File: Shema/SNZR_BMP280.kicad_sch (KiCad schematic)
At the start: 8 parts, among them J1 Conn_01x06_Pin, U1 BMP280

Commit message: izmjena koda i dodavanje simbola konektora u projekt
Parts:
- removed J1: Conn_01x06_Pin, symbol Connector:Conn_01x06_Pin
- added J1: ~, symbol Symbol_Library:Konektor
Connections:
- net +3.3V: now also J1.1 (3.3V)
- net CSB: now also J1.5 (CSB)
- net GND: now also J1.2 (GND)
- net SCL: now also J1.3 (SCL)
- net SDA: now also J1.4 (SDA)
- net SDO: now also J1.6 (SD0)
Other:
- note added: "3V3 GND SCL - PB8 SDA - PB9 Not Connected Not Connected"
- note added: "Nucleo"

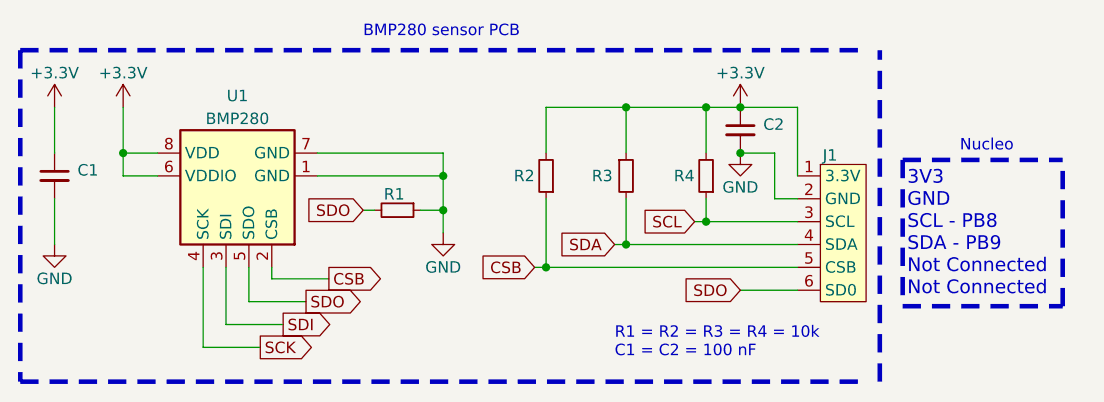
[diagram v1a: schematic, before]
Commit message: izmjenjen 3.3V na VCC na pinu konektora
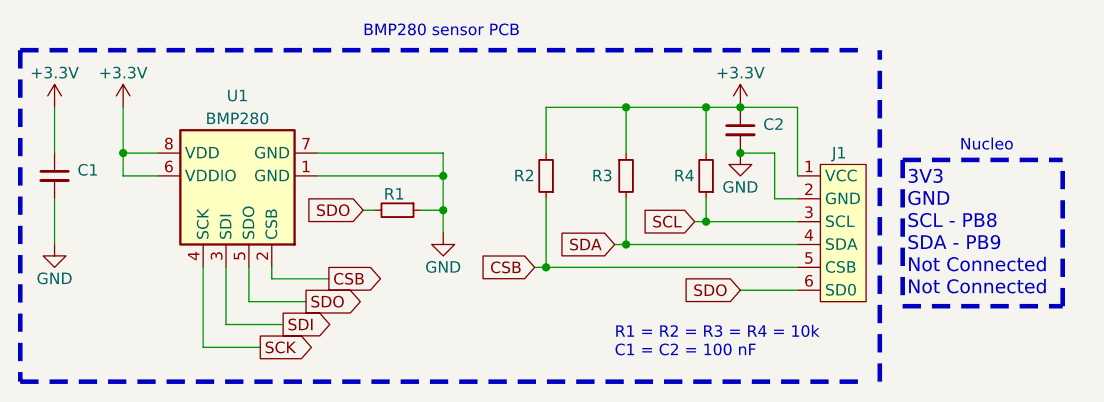
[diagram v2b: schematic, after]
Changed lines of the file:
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@@
+    )
+  )
+  (symbol (lib_name "Konektor_1") (lib_id "Symbol_Library:Konektor") (at 127 71.12 0) (unit 1)
+    (in_bom yes) (on_board yes) (dnp no)
+    (property "Reference" "J1" (at 125.73 62.23 0)
+      (effects (font (size 1.27 1.27)) (justify left))
+    )
+    (property "Value" "~" (at 121.92 60.96 0)
+      (effects (font (size 1.27 1.27)))
+    )
+    (property "Footprint" "" (at 121.92 60.96 0)
+      (effects (font (size 1.27 1.27)) hide)
+    )
+    (property "Datasheet" "" (at 121.92 60.96 0)
+      (effects (font (size 1.27 1.27)) hide)
+    )
+    (pin "1")
+    (pin "2")
+    (pin "3")
+    (pin "4")
+    (pin "5")
+    (pin "6")
+    (instances
+      (project "SNZR_BMP280"
+        (path "/09d5346e-2011-4469-84ee-b3a199e5e175"
+          (reference "J1") (unit 1)
+        )
+      )
     )
   )
@@
         )
       )
-    )
-  )
-  (symbol (lib_id "Symbol_Library:Konektor") (at 127 71.12 0) (unit 1)
-    (in_bom yes) (on_board yes) (dnp no)
-    (property "Reference" "J1" (at 124.714 62.484 0)
-      (effects (font (size 1.27 1.27)) (justify left))
-    )
-    (property "Value" "~" (at 121.92 60.96 0)
-      (effects (font (size 1.27 1.27)))
-    )
-    (property "Footprint" "" (at 121.92 60.96 0)
-      (effects (font (size 1.27 1.27)) hide)
-    )
-    (property "Datasheet" "" (at 121.92 60.96 0)
-      (effects (font (size 1.27 1.27)) hide)
-    )
-    (pin "1")
-    (pin "2")
-    (pin "3")
-    (pin "4")
-    (pin "5")
-    (pin "6")
-    (instances
-      (project "SNZR_BMP280"
-        (path "/09d5346e-2011-4469-84ee-b3a199e5e175"
-          (reference "J1") (unit 1)
-        )
-      )
